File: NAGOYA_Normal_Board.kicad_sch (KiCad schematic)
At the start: 93 parts, among them CN1 value, CN10 value, CN11 value, CN12 value, CN13 value, CN14 RefereeSystem, CN15 micro_B, CN2 value, CN3 value, CN4 value, CN5 value, CN6 value, CN7 value, CN8 value, CN9 value, J1 debug, Q2 DDTC114EUA-7-F, U1 Teensy4.1, U2 TCAN1042HVDR, U3 TCAN1042HVDR, U4 TCAN1042HVDR, U5 FT234XD, U6 TLP172AM, U7 BNO055, U9 LXES11DAA2-137, Y2 32.768 k

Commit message: Update
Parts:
- removed CN10, CN11, CN12, CN2, CN3, CN4, CN5, CN6, CN7, CN8, CN9: value, symbol 0_circuit:CON_2P
- removed U8: ~, TanekonModule:V-DFN3020-13-A_L3.0-W2.0-P0.45-BL-EP_AP6335X, symbol TanekonModule:AP63357DV-7
- added J10, J11, J12, J13, J14, J15, J16, J5, J6, J7, J8, J9: CAN3, Connector_JST:JST_GH_SM02B-GHS-TB_1x02-1MP_P1.25mm_Horizontal, symbol Connector_Generic_MountingPin:Conn_01x02_MountingPin
- added U10: AP63357, 0_PCB:V-DFN3020-13, symbol AP63357:AP63357
- CN1: value value -> XT30-M; footprint (none) -> 0_PCB:AMASS_XT30PW-M_1x02_P2.50mm_Horizontal; LCSC (none) -> C428721; 型番 (none) -> XT30PW-M30.G.Y; 購入先 (none) -> JLCPCB; 購入先URL (none) -> https://jlcpcb.com/partdetail/Changzhou_AmassElec-XT30UM/C9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; now fitted
- CN13: footprint (none) -> Connector_PinHeader_2.54mm:PinHeader_1x03_P2.54mm_Vertical
- CN14: footprint (none) -> Connector_JST:JST_XH_B3B-XH-AM_1x03_P2.50mm_Vertical
- CN15: footprint (none) -> Connector_USB:USB_Micro-B_Amphenol_10118194-0001LF_Horizontal
- F2: footprint (none) -> Fuse:Fuse_0603_1608Metric; LCSC (none) -> C116602
- L2: footprint (none) -> Inductor_SMD:L_0603_1608Metric; LCSC (none) -> C85834
- U9: footprint (none) -> 0_PCB:FIL_LXES11DAA2-137
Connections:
- net CAN1_H: now also J10.2 (Pin_2), J11.2 (Pin_2), J12.2 (Pin_2), J13.2 (Pin_2), J14.2 (Pin_2), J15.2 (Pin_2), J16.2 (Pin_2), J5.2 (Pin_2), J6.2 (Pin_2), J7.2 (Pin_2), J8.2 (Pin_2), J9.2 (Pin_2); no longer CN1.1
- net CAN1_L: now also J10.1 (Pin_1), J11.1 (Pin_1), J12.1 (Pin_1), J13.1 (Pin_1), J14.1 (Pin_1), J15.1 (Pin_1), J16.1 (Pin_1), J5.1 (Pin_1), J6.1 (Pin_1), J7.1 (Pin_1), J8.1 (Pin_1), J9.1 (Pin_1); no longer CN1.2
- net GND: now also CN1.1, J10.MP (MountPin), J11.MP (MountPin), J12.MP (MountPin), J13.MP (MountPin), J14.MP (MountPin), J15.MP (MountPin), J16.MP (MountPin), J5.MP (MountPin), J6.MP (MountPin), J7.MP (MountPin), J8.MP (MountPin), J9.MP (MountPin), U10.P$4 (COMP), U10.P$8 (GND)
- net at C14.1: now also U10.P$6 (BST)
- net at C14.2, L1.1: now also U10.P$7 (SW), U10.P$9 (SW)
- net at C15.2, R13.2, R14.1: now also U10.P$3 (FB)
- net +24V renamed V_BATT
- net V_BATT: now also CN1.2, U10.P$1 (VIN), U10.P$2 (EN)
- no-connect marks 25 -> 24
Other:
- moved on the sheet: C12, CN13

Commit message: PCBwo
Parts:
- removed C12, C13: 4.7u, Capacitor_SMD:C_1206_3216Metric, symbol Device:C
- removed C14: 0.1u(50V), Capacitor_SMD:C_0402_1005Metric, symbol Device:C
- removed C15: 47p, Capacitor_SMD:C_0402_1005Metric, symbol Device:C
- removed C16, C17: 22u, Resistor_SMD:R_1206_3216Metric, symbol Device:C
- removed D1: LED, LED_SMD:LED_0603_1608Metric, symbol Device:LED
- removed J11, J12, J15, J16: CAN3, Connector_JST:JST_GH_SM02B-GHS-TB_1x02-1MP_P1.25mm_Horizontal, symbol Connector_Generic_MountingPin:Conn_01x02_MountingPin
- removed L1: 6.8u, Inductor_SMD:L_TracoPower_TCK-047_5.2x5.8mm, symbol Device:L
- removed R1: 3.3k, Resistor_SMD:R_0603_1608Metric, symbol Device:R
- removed R14: 41.2k, Resistor_SMD:R_0201_0603Metric, symbol Device:R
- removed U10: AP63357, 0_PCB:V-DFN3020-13, symbol AP63357:AP63357
- removed ZD12: ESD5Z7.0T1G, Diode_SMD:D_SOD-523, symbol Diode:ESD5Zxx
- added C12, C13: 4.7u, Capacitor_SMD:C_1206_3216Metric, symbol Device:C_Small
- added C14: 100uF, Capacitor_SMD:CP_Elec_6.3x7.7, symbol Device:C_Polarized_Small
- added CN2: XT30-M, 0_PCB:AMASS_XT30U-M_1x02_P5.0mm_Vertical, symbol 0_circuit:CON_2P
- added CN3, CN4, CN5, CN6: XT30-F, 0_PCB:AMASS_XT30U-F_1x02_P5.0mm_Vertical, symbol 0_circuit:CON_2P
- added D6: LED, LED_SMD:LED_0603_1608Metric, symbol Device:LED
- added M78AR05-0.5: ~, 0_PCB:SIP3_LMS78-12_GAP, symbol 0_circuit:LMS78_2.0R
- added R5: 3.3k, Resistor_SMD:R_0603_1608Metric, symbol Device:R
- CN1: footprint 0_PCB:AMASS_XT30PW-M_1x02_P2.50mm_Horizontal -> 0_PCB:AMASS_XT30U-M_1x02_P5.0mm_Vertical
- R12: value 22k -> 4.7k; JLC https://jlcpcb.com/partdetail/18248-0805W8F2202T5E/C17560 -> https://jlcpcb.com/partdetail/18361-0805W8F4701T5E/C17673; LCSC C17560 -> C17673
- R13: value 220k -> 4.7k; footprint Resistor_SMD:R_0201_0603Metric -> Resistor_SMD:R_0805_2012Metric; JLC https://jlcpcb.com/partdetail/23688-0603WAF2203T5E/C22961 -> https://jlcpcb.com/partdetail/18361-0805W8F4701T5E/C17673; LCSC C22961 -> C17673
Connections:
- net VCC is gone; now on net +3.3V: JP2.1 (A), JP3.1 (A)
- net +3.3V: now also R12.1, R13.1
- net +5V: now also C13.1, C14.1, M78AR05-0.5.3 (Vo), R5.1; no longer R13.1
- net CAN1_H: no longer J10.2 (Pin_2), J13.2 (Pin_2), J14.2 (Pin_2), J9.2 (Pin_2), R3.2, R4.2, U3.7 (CANH), U4.7 (CANH), ZD4.1 (K), ZD5.1 (K)
- net CAN1_L: no longer J10.1 (Pin_1), J13.1 (Pin_1), J14.1 (Pin_1), J9.1 (Pin_1), R3.1, R4.1, U3.6 (CANL), U4.6 (CANL), ZD4.2 (K), ZD5.2 (K)
- net GND: now also C12.2, C13.2, C14.2, D6.1 (K), M78AR05-0.5.2 (GND); no longer R12.2
- net IMU_SCL: now also R12.2
- net IMU_SDA: now also R13.2
- net RX6: no longer J1.3 (Pin_3), ZD9.1 (K)
- net RX8: now also J1.3 (Pin_3), ZD9.1 (K)
- net TX6: no longer J1.4 (Pin_4), ZD8.1 (K)
- net TX8: now also J1.4 (Pin_4), ZD8.1 (K)
- net V_BATT: now also C12.1, M78AR05-0.5.1 (Vin); no longer R12.1
- new net: D6.2 (A), R5.2
- new net Ammo_GND: CN2.1, CN3.1, CN4.1, CN5.1, CN6.1
- new net CAN2_H: J10.2 (Pin_2), J9.2 (Pin_2), R3.2, U3.7 (CANH), ZD4.1 (K)
- new net CAN2_L: J10.1 (Pin_1), J9.1 (Pin_1), R3.1, U3.6 (CANL), ZD4.2 (K)
- new net CAN3_H: J13.2 (Pin_2), J14.2 (Pin_2), R4.2, U4.7 (CANH), ZD5.1 (K)
- new net CAN3_L: J13.1 (Pin_1), J14.1 (Pin_1), R4.1, U4.6 (CANL), ZD5.2 (K)
- new net V_Ammo: CN2.2, CN3.2, CN4.2, CN5.2, CN6.2
- no-connect marks 24 -> 23
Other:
- moved on the sheet: J13, J14

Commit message: Update
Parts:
- added D10, D8, D9: LED, LED_SMD:LED_0603_1608Metric, symbol Device:LED
- added Q4, Q5, Q6: DDTC114EUA-7-F, Package_TO_SOT_SMD:SOT-323_SC-70, symbol Transistor_BJT:DTC114E
- added R14, R16, R7: 3.3k, Resistor_SMD:R_0603_1608Metric, symbol Device:R
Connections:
- net +5V: now also R14.1, R16.1, R7.1
- net GND: now also C22.2, C23.1, C24.1, JP1.2 (B), R48.1, R49.1, U7.15 (GNDIO), U7.16 (GNDIO), U7.17 (COM3), U7.2 (GND), U7.25 (GNDIO), Q4.2 (E), Q5.2 (E), Q6.2 (E)
- net LED2: now reaches U1.30 (38)
- net LED2: now also Q4.1 (B)
- net LED3: now reaches U1.31 (39)
- net LED3: now also Q5.1 (B)
- net LED4: now reaches U1.32 (40)
- net LED4: now also Q6.1 (B)
- removed net GNDA: C22.2, C23.1, C24.1, C26.2, JP1.2 (B), R48.1, R49.1, U7.15 (GNDIO), U7.16 (GNDIO), U7.17 (COM3), U7.2 (GND), U7.25 (GNDIO), ZD11.2 (A)
- new net: D8.1 (K), Q4.3 (C)
- new net: D8.2 (A), R7.2
- new net: D9.2 (A), R14.2
- new net: C26.2, ZD11.2 (A)
- new net: D9.1 (K), Q5.3 (C)
- new net: D10.2 (A), R16.2
- new net: D10.1 (K), Q6.3 (C)
- no-connect marks 23 -> 20

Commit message: recommit
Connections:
- removed net Vio: C11.1, C7.1, C9.1, D2.1 (K), D3.1 (K), D4.1 (K), U2.5 (Vio), U3.5 (Vio), U4.5 (Vio)
- new net: C7.1, D2.1 (K), U2.5 (Vio)
- new net: C9.1, D3.1 (K), U3.5 (Vio)
- new net: C11.1, D4.1 (K), U4.5 (Vio)
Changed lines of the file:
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@@
-		)
-	)
-	(label "Vio"
-		(at 263.398 89.662 0)
-		(effects
-			(font
-				(size 1 1)
-			)
-			(justify left bottom)
-		)
-	)
-	(label "Vio"
-		(at 263.398 19.812 0)
-		(effects
-			(font
-				(size 1 1)
-			)
-			(justify left bottom)
-		)
-	)
-	(label "Vio"
-		(at 263.398 55.372 0)
-		(effects
-			(font
-				(size 1 1)
-			)
-			(justify left bottom)
 		)
 	)

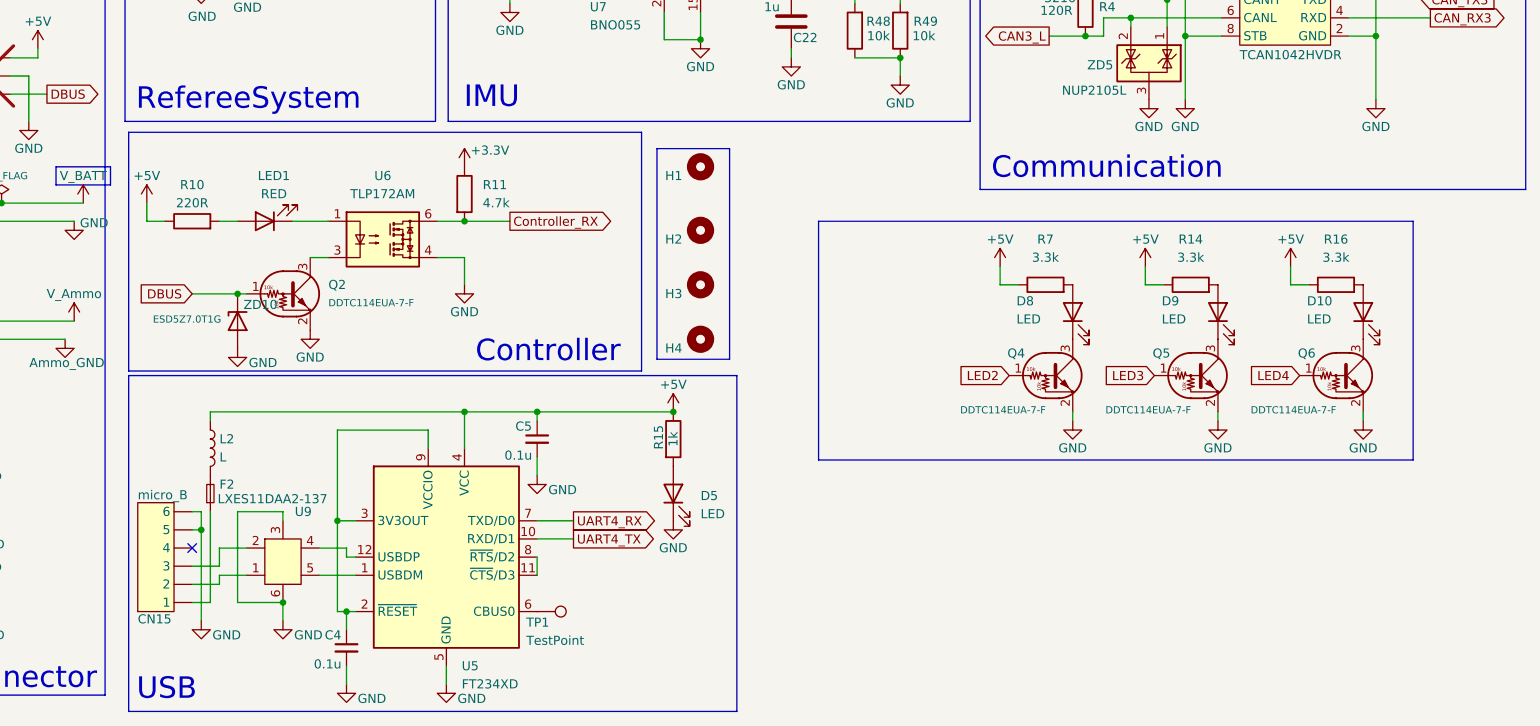
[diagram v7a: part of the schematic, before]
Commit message: USBシリアルを絶縁＞パターン変更
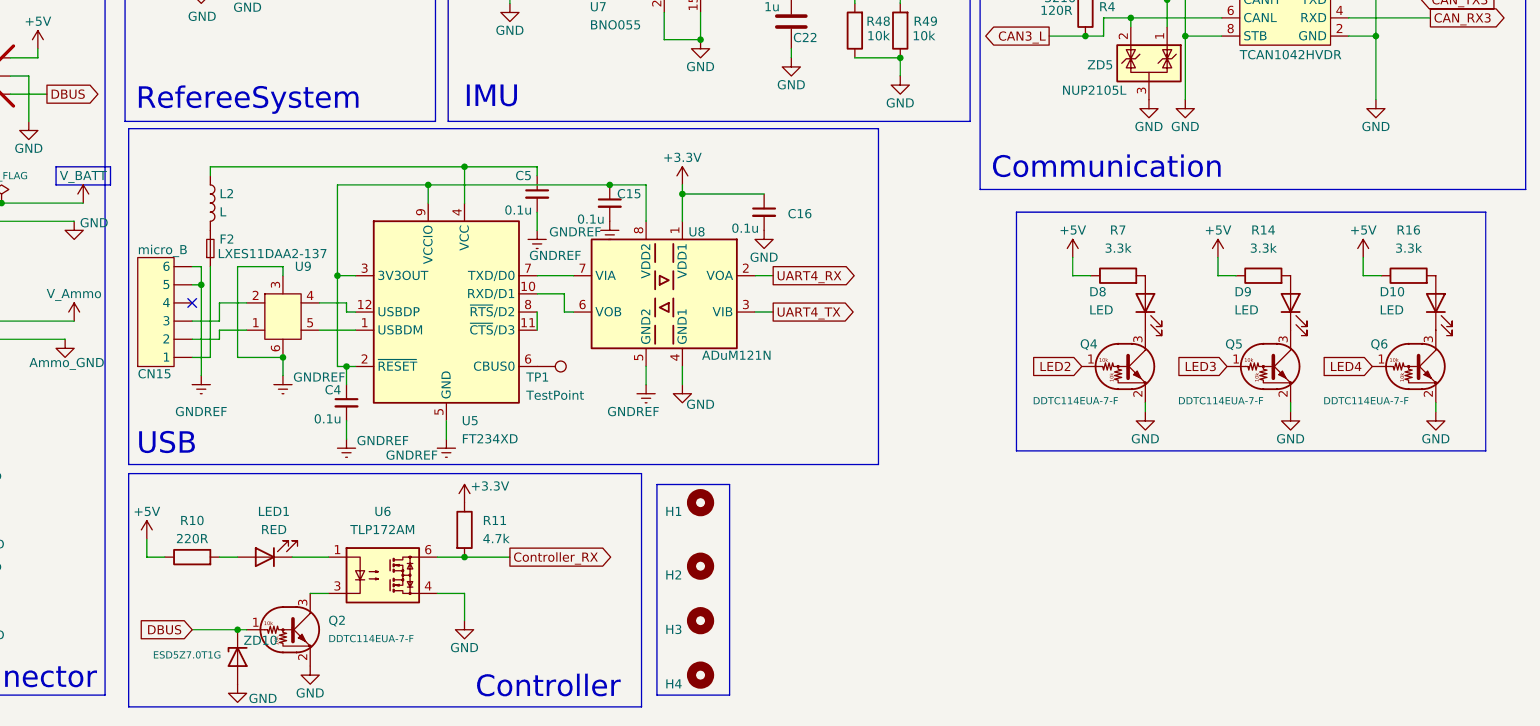
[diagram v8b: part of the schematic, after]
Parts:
- removed D5: LED, LED_SMD:LED_0603_1608Metric, symbol Device:LED
- removed R15: 1k, Resistor_SMD:R_0603_1608Metric, symbol Device:R
- added C15, C16: 0.1u, Capacitor_SMD:C_0603_1608Metric, symbol Device:C_Small
- added U8: ADuM121N, Package_SO:SOIC-8_3.9x4.9mm_P1.27mm, symbol Isolator:ADuM121N
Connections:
- net +3.3V: now also C16.1, U8.1 (VDD1)
- net +5V: no longer C5.1, L2.1, U5.4 (VCC)
- net GND: now also C16.2, U8.4 (GND1); no longer C4.2, C5.2, CN15.5, CN15.6, U5.13 (GND), U5.5 (GND), U9.3, U9.6
- net UART4_RX: now also U8.2 (VOA); no longer U5.7 (TXD/D0)
- net UART4_TX: now also U8.3 (VIB); no longer U5.10 (RXD/D1)
- net at C4.1, U5.2 (~{RESET}), U5.3 (3V3OUT)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: now also C15.1, U8.8 (VDD2)
- new net: U5.10 (RXD/D1), U8.6 (VOB)
- new net: C5.1, L2.1, U5.4 (VCC)
- new net: U5.7 (TXD/D0), U8.7 (VIA)
- new net GNDREF: C15.2, C4.2, C5.2, CN15.5, CN15.6, U5.13 (GND), U5.5 (GND), U8.5 (GND2), U9.3, U9.6
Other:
- moved on the sheet: C4, C5, CN15, D10, D8, D9, F2, H1, H2, H3, H4, L2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
